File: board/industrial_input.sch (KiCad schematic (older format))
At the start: 3 parts

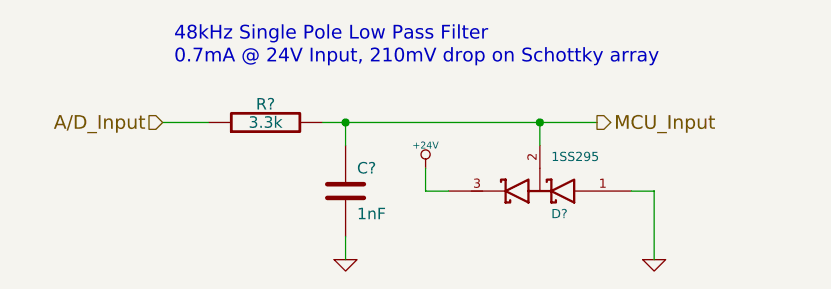
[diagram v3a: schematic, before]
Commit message: Fixed ERC Errors. Annotated all components.
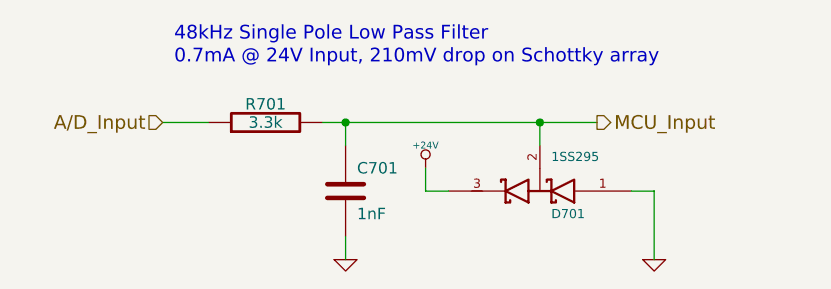
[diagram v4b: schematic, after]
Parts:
- gave numbers to parts that had none: 3
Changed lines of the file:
@@
 $Descr A 11000 8500
 encoding utf-8
-Sheet 14 26
+Sheet 7 26
 Title "Industrial Digital/Analog Input"
 Date ""
@@
 A/D_Input
 $Comp
-L R R?
+L R R701
 U 1 1 52E6DE87
 P 5400 3950
-F 0 "R?" V 5480 3950 50  0000 C CNN
+AR Path="/52F84966/52E6DE87" Ref="R701"  Part="1"
+AR Path="/52F85705/52E6DE87" Ref="R801"  Part="1"
+AR Path="/52F85B83/52E6DE87" Ref="R901"  Part="1"
+AR Path="/52F85B87/52E6DE87" Ref="R1001"  Part="1"
+AR Path="/52F8830D/52E6DE87" Ref="R1101"  Part="1"
+AR Path="/52F88311/52E6DE87" Ref="R1201"  Part="1"
+AR Path="/52F88315/52E6DE87" Ref="R1301"  Part="1"
+AR Path="/52F88319/52E6DE87" Ref="R1401"  Part="1"
+F 0 "R701" V 5480 3950 50  0000 C CNN
 F 1 "3.3k" V 5400 3950 50  0000 C CNN
 F 2 "" H 5400 3950 60  0000 C CNN
@@
 $EndComp
 $Comp
-L C C?
+L C C701
 U 1 1 52E6DEAB
 P 5750 4250
-F 0 "C?" H 5800 4350 50  0000 L CNN
+AR Path="/52F84966/52E6DEAB" Ref="C701"  Part="1"
+AR Path="/52F85705/52E6DEAB" Ref="C801"  Part="1"
+AR Path="/52F85B83/52E6DEAB" Ref="C901"  Part="1"
+AR Path="/52F85B87/52E6DEAB" Ref="C1001"  Part="1"
+AR Path="/52F8830D/52E6DEAB" Ref="C1101"  Part="1"
+AR Path="/52F88311/52E6DEAB" Ref="C1201"  Part="1"
+AR Path="/52F88315/52E6DEAB" Ref="C1301"  Part="1"
+AR Path="/52F88319/52E6DEAB" Ref="C1401"  Part="1"
+F 0 "C701" H 5800 4350 50  0000 L CNN
 F 1 "1nF" H 5800 4150 50  0000 L CNN
 F 2 "" H 5750 4250 60  0000 C CNN
@@
 $EndComp
 $Comp
-L GND #PWR?
+L GND #PWR0136
 U 1 1 52E6DEC4
 P 5750 4550
-F 0 "#PWR?" H 5750 4550 30  0001 C CNN
+AR Path="/52F84966/52E6DEC4" Ref="#PWR0136"  Part="1"
+AR Path="/52F85705/52E6DEC4" Ref="#PWR0139"  Part="1"
+AR Path="/52F85B83/52E6DEC4" Ref="#PWR0142"  Part="1"
+AR Path="/52F85B87/52E6DEC4" Ref="#PWR0145"  Part="1"
+AR Path="/52F8830D/52E6DEC4" Ref="#PWR0148"  Part="1"
+AR Path="/52F88311/52E6DEC4" Ref="#PWR0151"  Part="1"
+AR Path="/52F88315/52E6DEC4" Ref="#PWR0154"  Part="1"
+AR Path="/52F88319/52E6DEC4" Ref="#PWR0157"  Part="1"
+F 0 "#PWR0157" H 5750 4550 30  0001 C CNN
 F 1 "GND" H 5750 4480 30  0001 C CNN
 F 2 "" H 5750 4550 60  0000 C CNN
@@
 $EndComp
 $Comp
-L +24V #PWR?
+L +24V #PWR0137
 U 1 1 52E6DFBF
 P 6100 4150
-F 0 "#PWR?" H 6100 4100 20  0001 C CNN
+AR Path="/52F84966/52E6DFBF" Ref="#PWR0137"  Part="1"
+AR Path="/52F85705/52E6DFBF" Ref="#PWR0140"  Part="1"
+AR Path="/52F85B83/52E6DFBF" Ref="#PWR0143"  Part="1"
+AR Path="/52F85B87/52E6DFBF" Ref="#PWR0146"  Part="1"
+AR Path="/52F8830D/52E6DFBF" Ref="#PWR0149"  Part="1"
+AR Path="/52F88311/52E6DFBF" Ref="#PWR0152"  Part="1"
+AR Path="/52F88315/52E6DFBF" Ref="#PWR0155"  Part="1"
+AR Path="/52F88319/52E6DFBF" Ref="#PWR0158"  Part="1"
+F 0 "#PWR0158" H 6100 4100 20  0001 C CNN
 F 1 "+24V" H 6100 4250 30  0000 C CNN
 F 2 "" H 6100 4150 60  0000 C CNN
@@
 $EndComp
 $Comp
-L GND #PWR?
+L GND #PWR0138
 U 1 1 52E6DFEB
 P 7100 4550
-F 0 "#PWR?" H 7100 4550 30  0001 C CNN
+AR Path="/52F84966/52E6DFEB" Ref="#PWR0138"  Part="1"
+AR Path="/52F85705/52E6DFEB" Ref="#PWR0141"  Part="1"
+AR Path="/52F85B83/52E6DFEB" Ref="#PWR0144"  Part="1"
+AR Path="/52F85B87/52E6DFEB" Ref="#PWR0147"  Part="1"
+AR Path="/52F8830D/52E6DFEB" Ref="#PWR0150"  Part="1"
+AR Path="/52F88311/52E6DFEB" Ref="#PWR0153"  Part="1"
+AR Path="/52F88315/52E6DFEB" Ref="#PWR0156"  Part="1"
+AR Path="/52F88319/52E6DFEB" Ref="#PWR0159"  Part="1"
+F 0 "#PWR0159" H 7100 4550 30  0001 C CNN
 F 1 "GND" H 7100 4480 30  0001 C CNN
 F 2 "" H 7100 4550 60  0000 C CNN
@@
 $EndComp
 $Comp
-L DOUBLE_SCHOTTKY D?
+L DOUBLE_SCHOTTKY D701
 U 1 1 52E6E5BB
 P 6600 4250
-F 0 "D?" H 6550 4350 40  0000 R CNN
+AR Path="/52F84966/52E6E5BB" Ref="D701"  Part="1"
+AR Path="/52F85705/52E6E5BB" Ref="D801"  Part="1"
+AR Path="/52F85B83/52E6E5BB" Ref="D901"  Part="1"
+AR Path="/52F85B87/52E6E5BB" Ref="D1001"  Part="1"
+AR Path="/52F8830D/52E6E5BB" Ref="D1101"  Part="1"
+AR Path="/52F88311/52E6E5BB" Ref="D1201"  Part="1"
+AR Path="/52F88315/52E6E5BB" Ref="D1301"  Part="1"
+AR Path="/52F88319/52E6E5BB" Ref="D1401"  Part="1"
+F 0 "D701" H 6550 4350 40  0000 R CNN
 F 1 "1SS295" H 6550 4100 40  0000 R CNN
 F 2 "" H 6600 4250 60  0000 C CNN
